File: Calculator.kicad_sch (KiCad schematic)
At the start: 0 parts

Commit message: Added MCU & Decoupling Caps
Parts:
- added C1, C2, C3, C4, C5, C6: 0.1µF, Capacitor_SMD:C_0805_2012Metric_Pad1.18x1.45mm_HandSolder, symbol Device:C_Small
- added U1: STM32F205VGTx, Package_QFP:LQFP-100_14x14mm_P0.5mm, symbol MCU_ST_STM32F2:STM32F205VGTx
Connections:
- new net Vdd: C1.1, C2.1, C3.1, C4.1, C5.1, C6.1, U1.100 (VDD), U1.11 (VDD), U1.19 (VDD), U1.28 (VDD), U1.50 (VDD), U1.75 (VDD)
- new net Vss: C1.2, C2.2, C3.2, C4.2, C5.2, C6.2, U1.10 (VSS), U1.27 (VSS), U1.74 (VSS)
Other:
- note added: "+"
- note added: "-"

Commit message: Added SWL
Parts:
- added C7: 4.7µF, Capacitor_SMD:C_0603_1608Metric_Pad1.08x0.95mm_HandSolder, symbol Device:C
- added J1: Conn_01x05, Connector_PinHeader_2.54mm:PinHeader_1x05_P2.54mm_Vertical, symbol Connector_Generic:Conn_01x05
- added TP1: NRST, TestPoint:TestPoint_Pad_D1.0mm, symbol Connector:TestPoint
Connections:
- net Vdd: now also C6.2, U1.21 (VREF+), U1.22 (VDDA), U1.6 (VBAT), C7.1, J1.3 (Pin_3); no longer C6.1
- net Vss: now also C6.1, U1.20 (VSSA), C7.2, J1.4 (Pin_4); no longer C6.2
- net NRST: now reaches U1.14 (NRST)
- net NRST: now also J1.5 (Pin_5), TP1.1
- net SWDIO: now reaches U1.72 (PA13)
- net SWDIO: now also J1.1 (Pin_1)
- net SWCLK: now reaches U1.76 (PA14)
- net SWCLK: now also J1.2 (Pin_2)
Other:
- moved on the sheet: C6

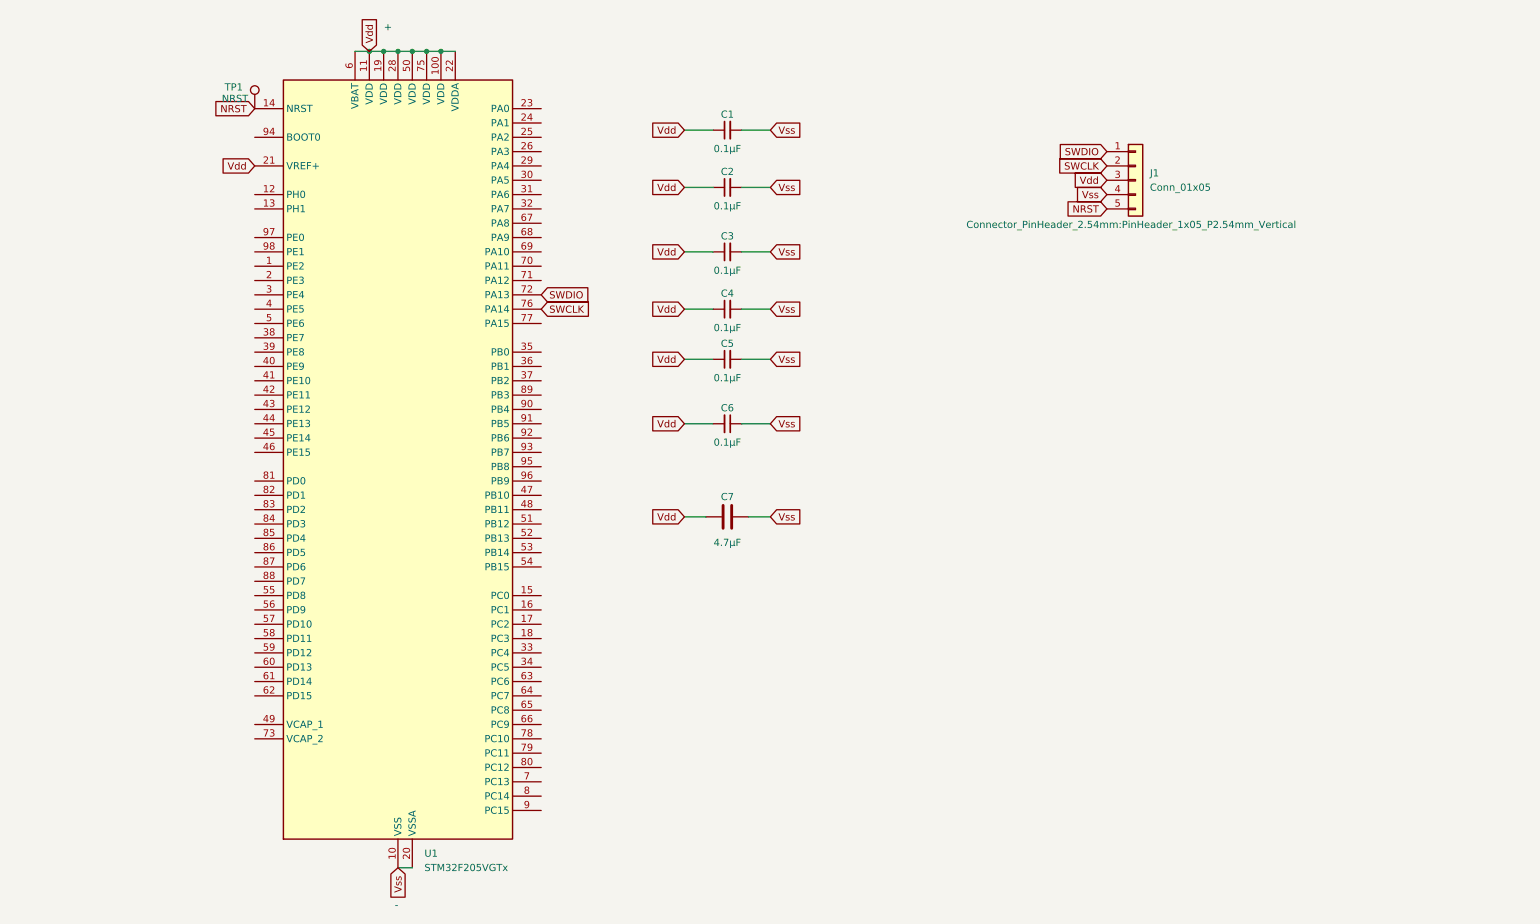
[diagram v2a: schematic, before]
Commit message: Added Display and Batteries
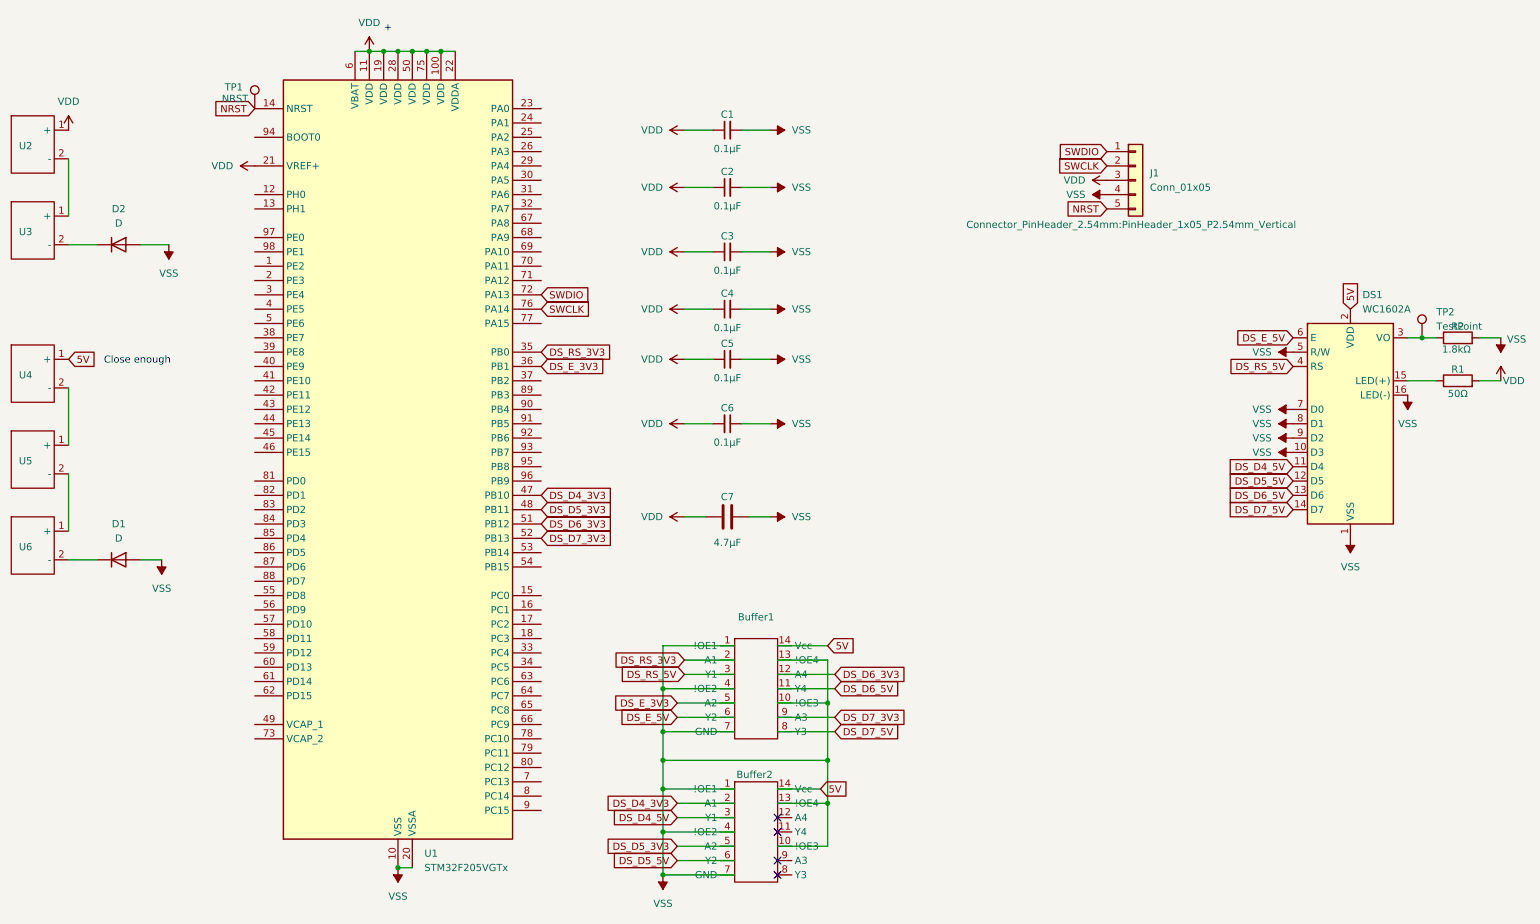
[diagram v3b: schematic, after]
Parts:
- added Buffer1, Buffer2: ~, Texas Instruments Logic Footprints:SNx4HCT125, symbol Texas Instrument Logic:SNx4HCT125
- added D1, D2: D, Diode_THT:D_DO-35_SOD27_P5.08mm_Vertical_KathodeUp, symbol Device:D
- added DS1: WC1602A, Display:WC1602A, symbol Display_Character:WC1602A
- added R1: 50Ω, Resistor_SMD:R_0805_2012Metric_Pad1.20x1.40mm_HandSolder, symbol Device:R
- added R2: 1.8kΩ, Resistor_SMD:R_0603_1608Metric_Pad0.98x0.95mm_HandSolder, symbol Device:R
- added TP2: TestPoint, TestPoint:TestPoint_Pad_D1.0mm, symbol Connector:TestPoint
- added U2, U3, U4, U5, U6: ~, CalcLibrary:BH-25C-1, symbol CalcLibrary:BH-25C-1
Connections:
- net DS_RS_3V3: now reaches U1.35 (PB0)
- net DS_RS_3V3: now also Buffer1.2 (A1)
- net DS_E_3V3: now reaches U1.36 (PB1)
- net DS_E_3V3: now also Buffer1.5 (A2)
- net DS_D4_3V3: now reaches U1.47 (PB10)
- net DS_D4_3V3: now also Buffer2.2 (A1)
- net DS_D5_3V3: now reaches U1.48 (PB11)
- net DS_D5_3V3: now also Buffer2.5 (A2)
- net DS_D6_3V3: now reaches U1.51 (PB12)
- net DS_D6_3V3: now also Buffer1.12 (A4)
- net DS_D7_3V3: now reaches U1.52 (PB13)
- net DS_D7_3V3: now also Buffer1.9 (A3)
- net Vdd renamed VDD
- net VDD: now also R1.2, U2.1 (+)
- net Vss renamed VSS
- net VSS: now also Buffer1.1 (!OE1), Buffer1.10 (!OE3), Buffer1.13 (!OE4), Buffer1.4 (!OE2), Buffer1.7 (GND), Buffer2.1 (!OE1), Buffer2.10 (!OE3), Buffer2.13 (!OE4), Buffer2.4 (!OE2), Buffer2.7 (GND), D1.2 (A), D2.2 (A), DS1.1 (VSS), DS1.10 (D3), DS1.16 (LED(-)), DS1.5 (R/W), DS1.7 (D0), DS1.8 (D1), DS1.9 (D2), R2.2
- new net: DS1.3 (VO), R2.1, TP2.1
- new net: U4.2 (-), U5.1 (+)
- new net: DS1.15 (LED(+)), R1.1
- new net: D1.1 (K), U6.2 (-)
- new net: D2.1 (K), U3.2 (-)
- new net: U5.2 (-), U6.1 (+)
- new net: U2.2 (-), U3.1 (+)
- new net 5V: Buffer1.14 (Vcc), Buffer2.14 (Vcc), DS1.2 (VDD), U4.1 (+)
- new net DS_D4_5V: Buffer2.3 (Y1), DS1.11 (D4)
- new net DS_D5_5V: Buffer2.6 (Y2), DS1.12 (D5)
- new net DS_D6_5V: Buffer1.11 (Y4), DS1.13 (D6)
- new net DS_D7_5V: Buffer1.8 (Y3), DS1.14 (D7)
- new net DS_E_5V: Buffer1.6 (Y2), DS1.6 (E)
- new net DS_RS_5V: Buffer1.3 (Y1), DS1.4 (RS)
- no-connect marks 0 -> 4
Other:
- note added: "Close enough"
- note removed: "-"
